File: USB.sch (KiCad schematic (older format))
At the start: 4 parts, among them J901 USB_B_Micro

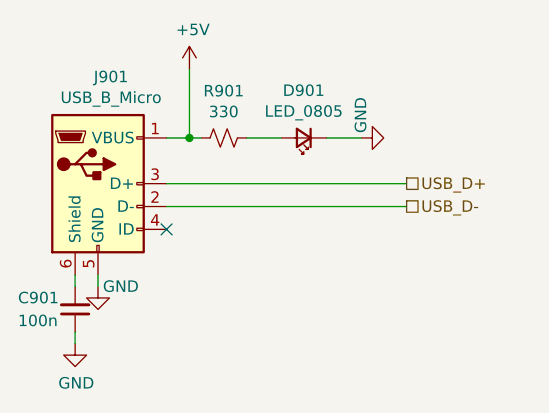
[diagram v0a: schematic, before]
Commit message: Submited for production & smt assembly
v0.01
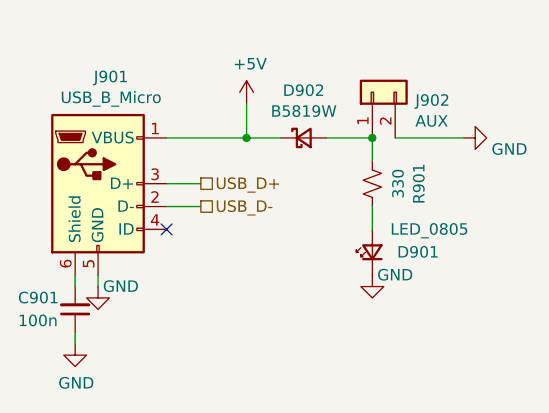
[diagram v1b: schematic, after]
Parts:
- added D902: B5819W, Diode_SMD:D_SOD-123, symbol Device:D_Schottky_Small
- added J902: AUX, Connector_PinHeader_2.54mm:PinHeader_1x02_P2.54mm_Vertical, symbol Connector_Generic:Conn_01x02
- C901: footprint (none) -> Capacitor_SMD:C_0402_1005Metric
- D901: footprint (none) -> LED_SMD:LED_0805_2012Metric
- J901: footprint (none) -> Connector_USB:USB_Micro-B_Amphenol_10104110_Horizontal
- R901: footprint (none) -> Resistor_SMD:R_0402_1005Metric
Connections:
- net +5V: now also D902.1 (K); no longer R901.2
- net GND: now also J902.2 (Pin_2)
- new net: D902.2 (A), J902.1 (Pin_1), R901.2
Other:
- moved on the sheet: D901, R901
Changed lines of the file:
@@
 $Descr A4 11693 8268
 encoding utf-8
-Sheet 9 10
+Sheet 8 10
 Title ""
 Date ""
@@
 F 0 "J901" H 4957 3667 50  0000 C CNN
 F 1 "USB_B_Micro" H 4957 3576 50  0000 C CNN
-F 2 "" H 5050 3150 50  0001 C CNN
+F 2 "Connector_USB:USB_Micro-B_Amphenol_10104110_Horizontal" H 5050 3150 50  0001 C CNN
 F 3 "~" H 5050 3150 50  0001 C CNN
 	1    4900 3200
@@
 F 0 "C901" H 5050 3700 50  0000 R CNN
 F 1 "100n" H 5050 3800 50  0000 R CNN
-F 2 "" H 4800 3750 50  0001 C CNN
+F 2 "Capacitor_SMD:C_0402_1005Metric" H 4800 3750 50  0001 C CNN
 F 3 "~" H 4800 3750 50  0001 C CNN
 	1    4800 3750
@@
 	4800 3650 4800 3600
 Wire Wire Line
-	5200 3200 6250 3200
+	5200 3200 5350 3200
 Wire Wire Line
-	5200 3300 6250 3300
-Text HLabel 6250 3200 2    50   UnSpc ~ 0
+	5200 3300 5350 3300
+Text HLabel 5350 3200 2    50   UnSpc ~ 0
 USB_D+
-Text HLabel 6250 3300 2    50   UnSpc ~ 0
+Text HLabel 5350 3300 2    50   UnSpc ~ 0
 USB_D-
 NoConn ~ 5200 3400
@@
 L Device:R_Small_US R901
 U 1 1 5EFE2814
-P 5450 3000
-F 0 "R901" V 5245 3000 50  0000 C CNN
-F 1 "330" V 5336 3000 50  0000 C CNN
-F 2 "" H 5450 3000 50  0001 C CNN
-F 3 "~" H 5450 3000 50  0001 C CNN
-	1    5450 3000
-	0    1    1    0
+P 6100 3200
+F 0 "R901" V 5895 3200 50  0000 C CNN
+F 1 "330" V 5986 3200 50  0000 C CNN
+F 2 "Resistor_SMD:R_0402_1005Metric" H 6100 3200 50  0001 C CNN
+F 3 "~" H 6100 3200 50  0001 C CNN
+	1    6100 3200
+	-1   0    0    1
 $EndComp
 $Comp
 L Device:LED_Small D901
 U 1 1 5EFE2C42
-P 5800 3000
-F 0 "D901" H 5800 2793 50  0000 C CNN
-F 1 "LED_0805" H 5800 2884 50  0000 C CNN
-F 2 "" V 5800 3000 50  0001 C CNN
-F 3 "~" V 5800 3000 50  0001 C CNN
-	1    5800 3000
-	-1   0    0    1
+P 6100 3500
+F 0 "D901" V 6100 3300 50  0000 C CNN
+F 1 "LED_0805" V 6200 3250 50  0000 C CNN
+F 2 "LED_SMD:LED_0805_2012Metric" V 6100 3500 50  0001 C CNN
+F 3 "~" V 6100 3500 50  0001 C CNN
+	1    6100 3500
+	0    -1   -1   0
 $EndComp
-Wire Wire Line
-	5350 3000 5300 3000
-Wire Wire Line
-	5550 3000 5700 3000
-Wire Wire Line
-	5900 3000 6050 3000
 $Comp
 L power:GND #PWR0904
 U 1 1 5EFE3360
-P 6050 3000
-F 0 "#PWR0904" H 6050 2750 50  0001 C CNN
-F 1 "GND" H 6150 3000 50  0000 C CNN
-F 2 "" H 6050 3000 50  0001 C CNN
-F 3 "" H 6050 3000 50  0001 C CNN
-	1    6050 3000
-	0    -1   -1   0
+P 6100 3600
+F 0 "#PWR0904" H 6100 3350 50  0001 C CNN
+F 1 "GND" H 6200 3600 50  0000 C CNN
+F 2 "" H 6100 3600 50  0001 C CNN
+F 3 "" H 6100 3600 50  0001 C CNN
+	1    6100 3600
+	1    0    0    -1
 $EndComp
 Wire Wire Line
-	5300 3000 5300 2700
-Connection ~ 5300 3000
+	5550 3000 5550 2850
 Wire Wire Line
-	5300 3000 5200 3000
+	5550 3000 5200 3000
 $Comp
 L power:+5V #PWR0903
 U 1 1 5EFE3C47
-P 5300 2700
-F 0 "#PWR0903" H 5300 2550 50  0001 C CNN
-F 1 "+5V" H 5315 2873 50  0000 C CNN
-F 2 "" H 5300 2700 50  0001 C CNN
-F 3 "" H 5300 2700 50  0001 C CNN
-	1    5300 2700
+P 5550 2850
+F 0 "#PWR0903" H 5550 2700 50  0001 C CNN
+F 1 "+5V" H 5565 3023 50  0000 C CNN
+F 2 "" H 5550 2850 50  0001 C CNN
+F 3 "" H 5550 2850 50  0001 C CNN
+	1    5550 2850
 	1    0    0    -1
 $EndComp
 Wire Wire Line
 	4900 3650 4900 3600
+$Comp
+L Connector_Generic:Conn_01x02 J902
+U 1 1 5EF3060A
+P 6100 2800
+F 0 "J902" V 6064 2612 50  0000 R CNN
+F 1 "AUX" V 5973 2612 50  0000 R CNN
+F 2 "Connector_PinHeader_2.54mm:PinHeader_1x02_P2.54mm_Vertical" H 6100 2800 50  0001 C CNN
+F 3 "~" H 6100 2800 50  0001 C CNN
+	1    6100 2800
+	0    -1   -1   0
+$EndComp
+Wire Wire Line
+	6100 3100 6100 3000
+Wire Wire Line
+	6100 3400 6100 3300
+$Comp
+L power:GND #PWR0905
+U 1 1 5EF348ED
+P 6500 3000
+F 0 "#PWR0905" H 6500 2750 50  0001 C CNN
+F 1 "GND" V 6450 2800 50  0000 C CNN
+F 2 "" H 6500 3000 50  0001 C CNN
+F 3 "" H 6500 3000 50  0001 C CNN
+	1    6500 3000
+	0    -1   -1   0
+$EndComp
+$Comp
+L Device:D_Schottky_Small D902
+U 1 1 5EF363E2
+P 5800 3000
+F 0 "D902" H 5800 3207 50  0000 C CNN
+F 1 "B5819W" H 5800 3116 50  0000 C CNN
+F 2 "Diode_SMD:D_SOD-123" V 5800 3000 50  0001 C CNN
+F 3 "~" V 5800 3000 50  0001 C CNN
+	1    5800 3000
+	1    0    0    -1
+$EndComp
+Wire Wire Line
+	5550 3000 5700 3000
+Connection ~ 5550 3000
+Wire Wire Line
+	5900 3000 6100 3000
+Connection ~ 6100 3000
+Wire Wire Line
+	6200 3000 6500 3000
 $EndSCHEMATC
